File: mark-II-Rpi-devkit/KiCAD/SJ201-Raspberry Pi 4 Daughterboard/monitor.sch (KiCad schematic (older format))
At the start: 0 parts

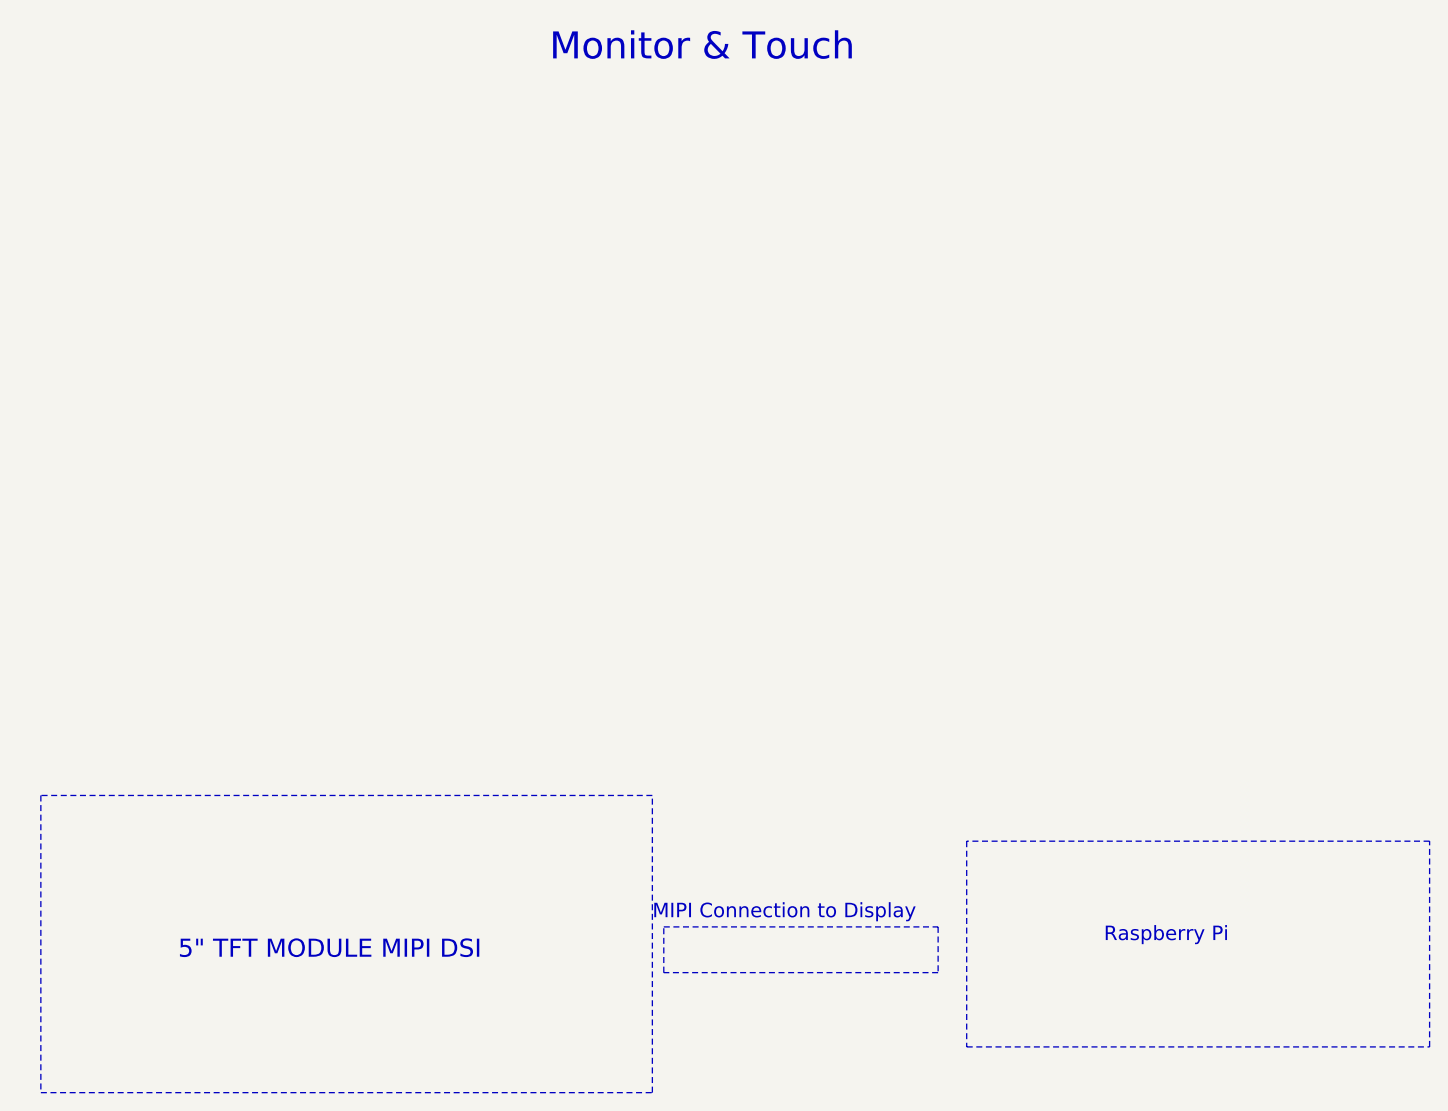
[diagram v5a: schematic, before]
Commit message: SJ201 - Removed CM108b soundcard, added in I2S to Line out, ATTin402. Moved holes in layout. SJ202 - extened length to plug into USB2.0 port
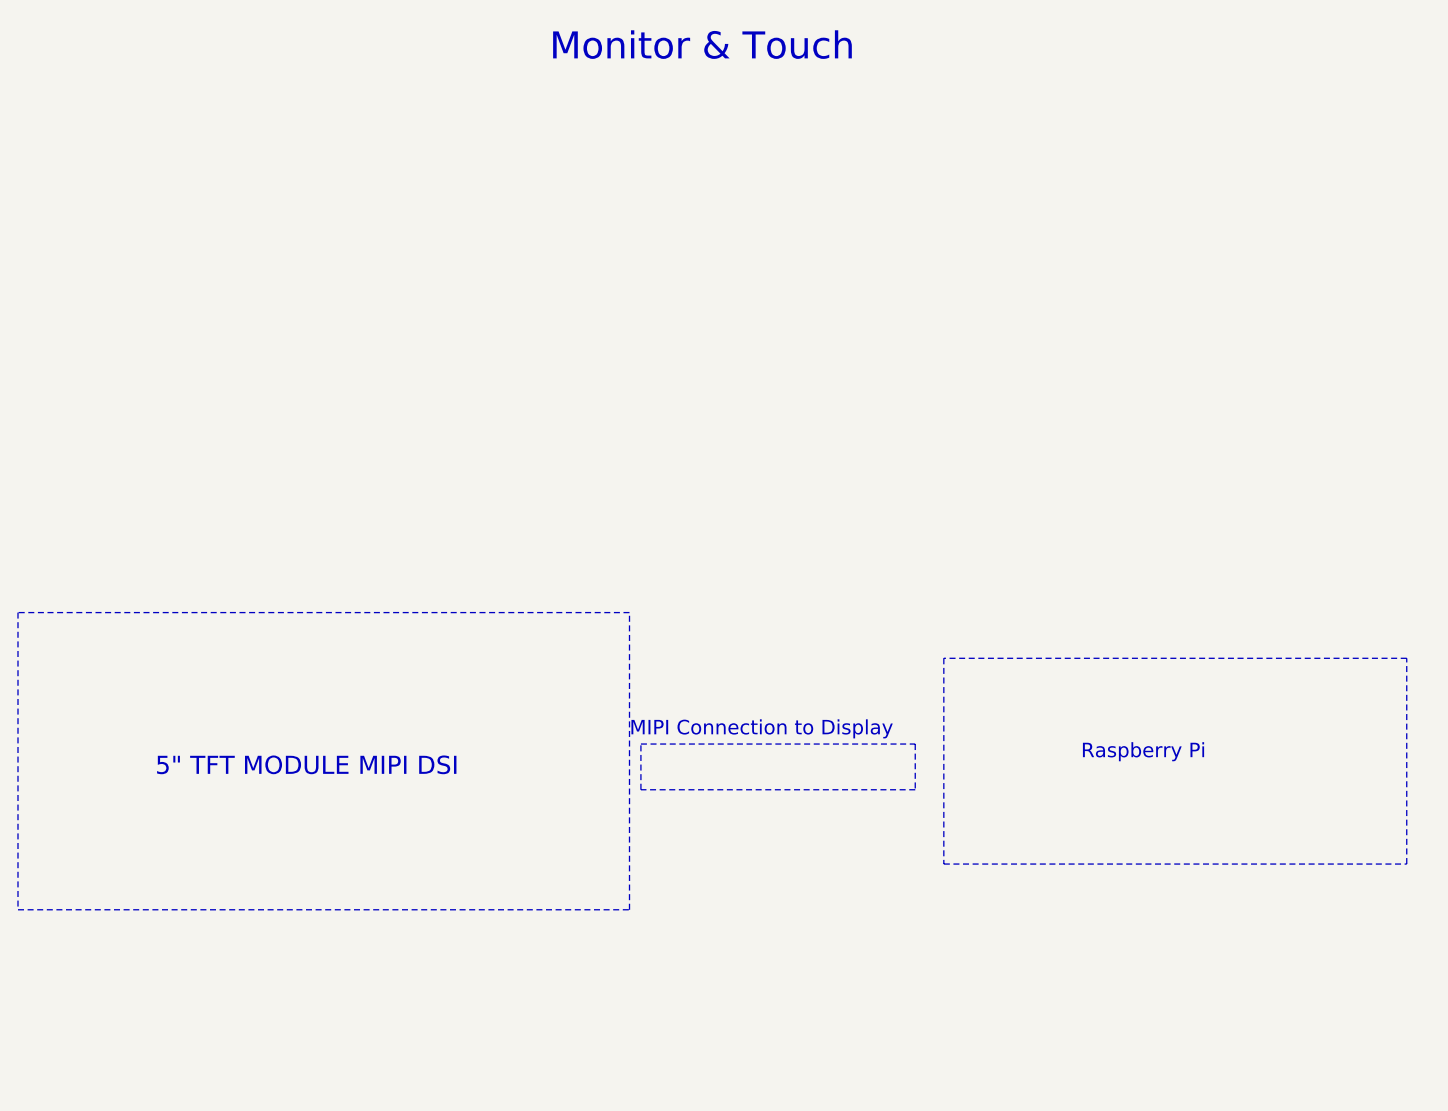
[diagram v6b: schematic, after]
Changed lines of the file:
@@
 Sheet 4 6
 Title ""
-Date "2020-08-16"
-Rev "0.66"
+Date "2020-09-26"
+Rev "0.67b"
 Comp ""
 Comment1 ""
@@
 Text Notes 4725 875  0    118  ~ 0
 Monitor & Touch
+Text Notes 7050 3925 0    63   ~ 0
+Raspberry Pi
+Text Notes 5075 3825 0    63   ~ 0
+MIPI Connection to Display
 Wire Notes Line
-	2500 4075 2500 5375
+	5125 4050 5125 3850
 Wire Notes Line
-	2500 5375 5175 5375
+	6325 4050 5125 4050
 Wire Notes Line
-	5175 5375 5175 4075
+	6325 3850 6325 4050
 Wire Notes Line
-	5175 4075 2500 4075
-Text Notes 3100 4800 0    79   ~ 0
+	5125 3850 6325 3850
+Wire Notes Line
+	8475 3475 6450 3475
+Wire Notes Line
+	8475 4375 8475 3475
+Wire Notes Line
+	6450 4375 8475 4375
+Wire Notes Line
+	6450 3475 6450 4375
+Text Notes 3000 4000 0    79   ~ 0
 5" TFT MODULE MIPI DSI
 Wire Notes Line
-	6550 4275 6550 5175
+	5075 3275 2400 3275
 Wire Notes Line
-	6550 5175 8575 5175
+	5075 4575 5075 3275
 Wire Notes Line
-	8575 5175 8575 4275
+	2400 4575 5075 4575
 Wire Notes Line
-	8575 4275 6550 4275
-Wire Notes Line
-	5225 4650 6425 4650
-Wire Notes Line
-	6425 4650 6425 4850
-Wire Notes Line
-	6425 4850 5225 4850
-Wire Notes Line
-	5225 4850 5225 4650
-Text Notes 5175 4625 0    63   ~ 0
-MIPI Connection to Display
-Text Notes 7150 4725 0    63   ~ 0
-Raspberry Pi
+	2400 3275 2400 4575
 $EndSCHEMATC
